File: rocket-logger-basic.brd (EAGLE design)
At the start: 58.5 x 62 mm, 57 parts, among them IC1 CC430F513X, Q2 MOSFET-PCHANNEL, U1 MAX1555, U2 MAX1555, X1 0896BM15A0001, X2 USB-MICROB, X3 SMA-142-0701-801/806

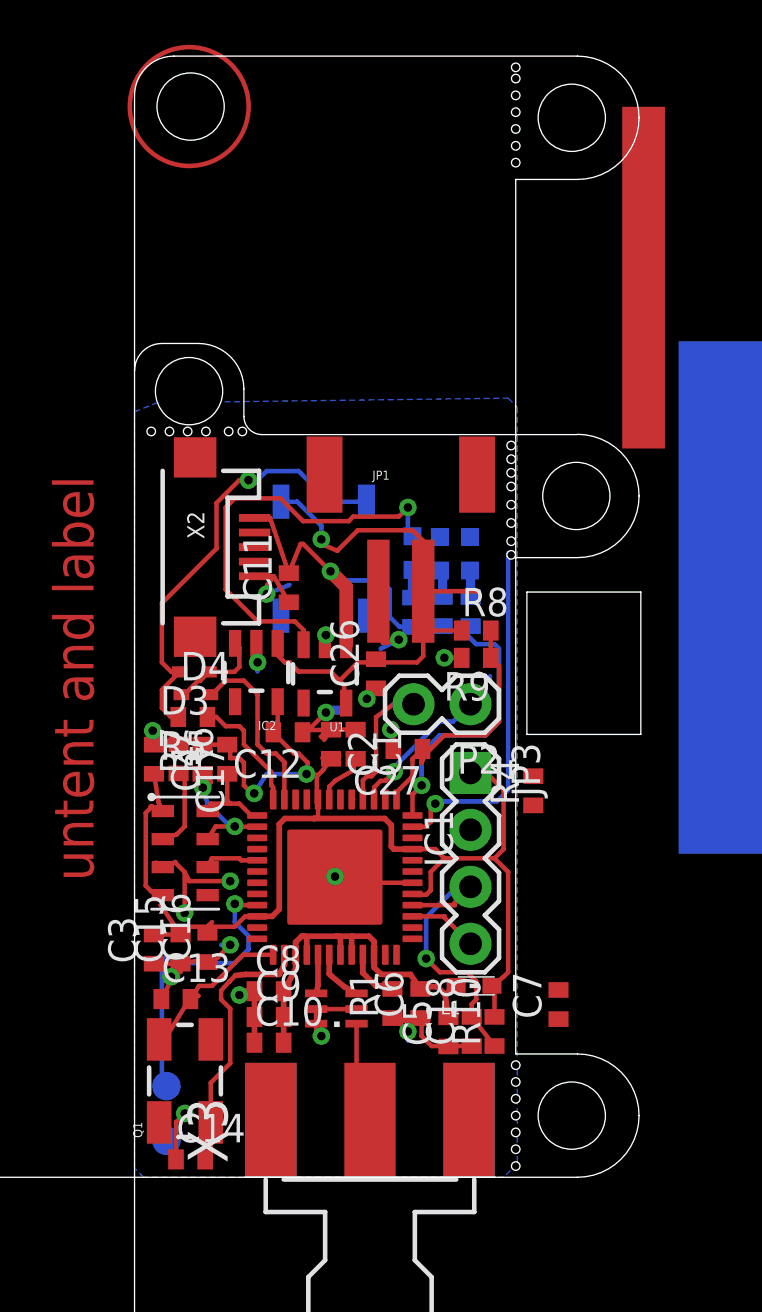
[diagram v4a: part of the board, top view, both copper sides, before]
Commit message: switched to smaller jst connector and done routing
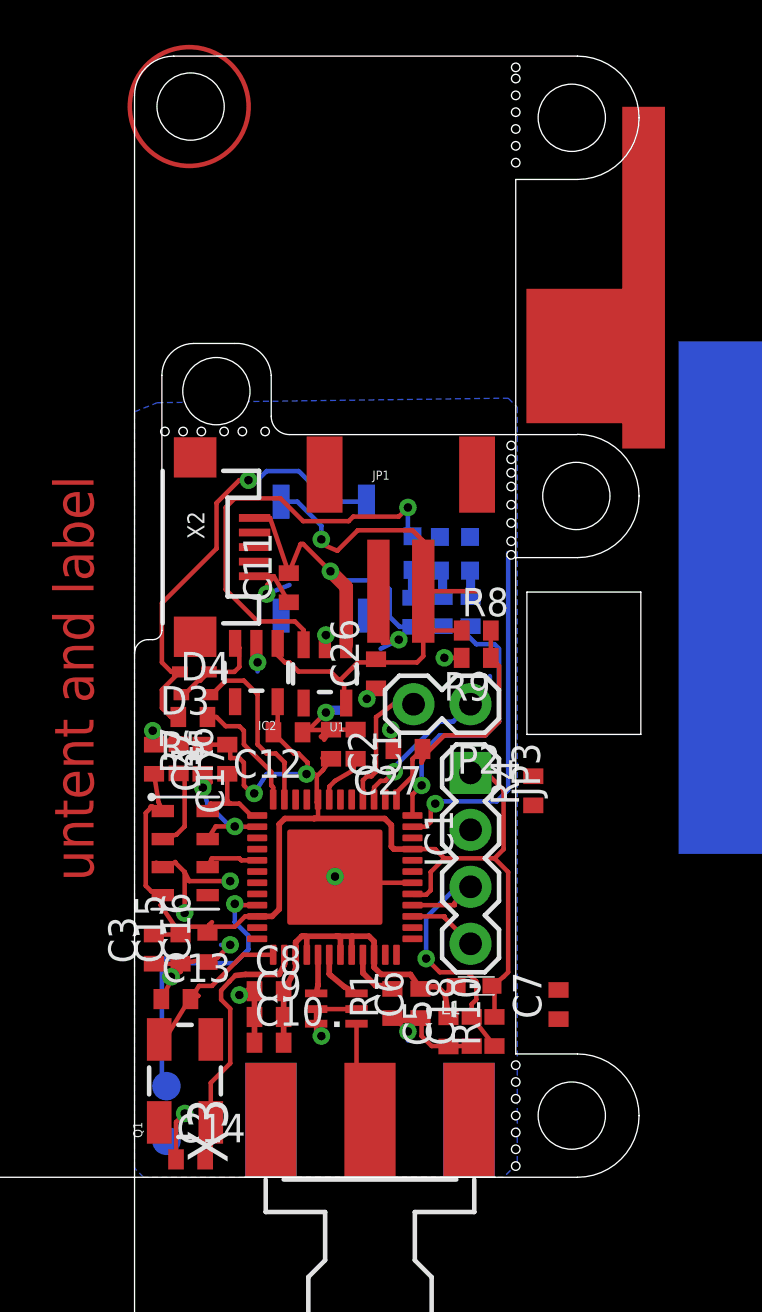
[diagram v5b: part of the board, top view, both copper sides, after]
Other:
- outline, holes or cut-outs redrawn
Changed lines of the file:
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@@
 <text x="10.25" y="37.75" size="1.016" layer="122" ratio="12" rot="MR270">ON</text>
 <text x="8.5" y="37.75" size="1.016" layer="122" ratio="12" rot="MR270">ACT</text>
-<wire x1="0" y1="48.25" x2="0" y2="35.9664" width="0" layer="20"/>
-<wire x1="0" y1="35.9664" x2="0" y2="0" width="0" layer="20"/>
+<wire x1="0" y1="48.25" x2="0" y2="23.368" width="0" layer="20"/>
+<wire x1="0" y1="23.368" x2="0" y2="0" width="0" layer="20"/>
 <wire x1="22.5" y1="2.75" x2="19.75" y2="0" width="0" layer="20" curve="-90"/>
 <wire x1="19.75" y1="5.5" x2="22.5" y2="2.75" width="0" layer="20" curve="-90"/>
@@
 <circle x="2.4384" y="47.752" radius="2.649403125" width="0.2032" layer="1"/>
 <text x="-1.8288" y="13.208" size="1.778" layer="1" rot="R90">untent and label</text>
-<hole x="2.4312" y="35.0588" drill="3"/>
-<wire x1="0" y1="35.9664" x2="1.2192" y2="37.1856" width="0" layer="20" curve="-90"/>
-<wire x1="1.2192" y1="37.1856" x2="2.8448" y2="37.1856" width="0" layer="20"/>
-<wire x1="2.8448" y1="37.1856" x2="4.8768" y2="35.1536" width="0" layer="20" curve="-90"/>
-<wire x1="4.8768" y1="35.1536" x2="4.8768" y2="33.9344" width="0" layer="20"/>
-<wire x1="4.8768" y1="33.9344" x2="5.6896" y2="33.1216" width="0" layer="20" curve="90"/>
-<wire x1="5.6896" y1="33.1216" x2="17.0688" y2="33.1216" width="0" layer="20"/>
+<hole x="3.6504" y="35.0588" drill="3"/>
+<wire x1="2.6416" y1="37.1856" x2="4.4704" y2="37.1856" width="0" layer="20"/>
+<wire x1="4.4704" y1="37.1856" x2="6.096" y2="35.7632" width="0" layer="20" curve="-90"/>
+<wire x1="6.096" y1="35.7632" x2="6.096" y2="33.9344" width="0" layer="20"/>
+<wire x1="6.096" y1="33.9344" x2="6.9088" y2="33.1216" width="0" layer="20" curve="90"/>
+<wire x1="6.9088" y1="33.1216" x2="17.0688" y2="33.1216" width="0" layer="20"/>
+<hole x="5.824" y="33.2612" drill="0.381"/>
 <hole x="4.808" y="33.2612" drill="0.381"/>
-<hole x="4.1984" y="33.2612" drill="0.381"/>
-<hole x="3.1824" y="33.2612" drill="0.381"/>
-<hole x="2.3696" y="33.2612" drill="0.381"/>
-<hole x="1.5568" y="33.2612" drill="0.381"/>
-<hole x="0.744" y="33.2612" drill="0.381"/>
+<hole x="3.9952" y="33.2612" drill="0.381"/>
+<hole x="2.9792" y="33.2612" drill="0.381"/>
+<hole x="2.1664" y="33.2612" drill="0.381"/>
+<hole x="1.3536" y="33.2612" drill="0.381"/>
 <wire x1="19.75" y1="33.1208" x2="17" y2="33.1208" width="0" layer="20"/>
 <wire x1="19.75" y1="33.1344" x2="22.5" y2="30.3844" width="0" layer="20" curve="-90"/>
@@
 <dimension x1="0" y1="0" x2="0" y2="33.1216" x3="-20.7264" y3="16.5608" layer="16"/>
 <dimension x1="0" y1="0" x2="17.0688" y2="0" x3="8.5344" y3="-15.6464" layer="16"/>
+<rectangle x1="17.4752" y1="33.6296" x2="21.9964" y2="39.624" layer="1" rot="R180"/>
+<dimension x1="0" y1="0" x2="0" y2="37.1856" x3="-27.2288" y3="18.5928" layer="16"/>
+<wire x1="1.2192" y1="24.384" x2="0.8128" y2="23.9776" width="0" layer="20" curve="-90"/>
+<wire x1="0.8128" y1="23.9776" x2="0.6096" y2="23.9776" width="0" layer="20"/>
+<wire x1="0.6096" y1="23.9776" x2="0" y2="23.368" width="0" layer="20" curve="90"/>
+<wire x1="1.2192" y1="24.384" x2="1.2192" y2="35.7632" width="0" layer="20"/>
+<wire x1="1.2192" y1="35.7632" x2="2.6416" y2="37.1856" width="0" layer="20" curve="-90"/>
 </plain>
 <attributes>

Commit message: some routing done, changed lipo charger
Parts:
- removed U1: MAX1555, SparkFun:SOT23-5
- added C19: (no value), resistor:C0402
- added R13: (no value), rcl:R0402
- added U$1: JST-ZR-2, Mine:JST-ZR-2
- added U$2: JST-ZR-2SMD, Mine:JST-ZR-2-SMD
- added U3: MCP73831, SparkFun-PowerIC:SOT23-5
- moved JP1 29.6 mm to (34.8, 48.5)
- moved C27 6.10 mm to (15.2, 24.4)
- moved LED1 4.72 mm to (12.0, 24.2), turned to 270 degrees
- moved S2 3.41 mm to (5.53, 29.4), turned to 180 degrees
- moved LED2 2.96 mm to (12.0, 25.4), turned to 270 degrees
- moved C12 2.54 mm to (7.60, 22.3), turned to 90 degrees
- moved R11 2.20 mm to (14.2, 26.4), turned to 180 degrees
- moved C26 1.94 mm to (8.84, 22.3)
- moved LED3 1.48 mm to (12.0, 26.4), turned to 270 degrees
- moved R2 1.36 mm to (14.2, 24.1), turned to 0 degrees
- moved R8 1.22 mm to (15.2, 25.6)
- moved C11 1.12 mm to (7.59, 25.4)
- moved R3 0.46 mm to (14.2, 25.3), turned to 0 degrees
- moved R6 0.41 mm to (4.54, 18.6)
- moved IC2 0.20 mm to (5.43, 22.3)
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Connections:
- new net N$1: R13.1, U3.5
- net +3V3: now also C19.2
- net GND: now also C19.1, R13.2, U$1.2, U$2.2, U3.2; no longer U1.2
- net N$18: now also U3.4; no longer U1.1
- net N$19: now also U3.1; no longer U1.3
- net N$2: now also U$1.1, U$2.1, U3.3; no longer U1.5
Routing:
- net N$19: track 18.9 -> 0.00 mm, vias 1 -> 0
- net GND: track 54.0 -> 60.2 mm, vias 18 -> 16
- net N$24: track 19.9 -> 25.4 mm
- net N$18: track 15.6 -> 19.3 mm
- net +3V3: track 62.3 -> 64.0 mm
- net N$10: track 1.30 -> 0.00 mm
- net N$2: track 26.7 -> 28.0 mm
- net N$15: track 1.24 -> 0.00 mm
- net N$9: track 1.20 -> 0.00 mm
- net N$17: track 15.9 -> 14.7 mm
- net N$1: track 0.00 -> 0.99 mm
- net N$12: track 5.90 -> 5.30 mm
- net N$11: track 6.50 -> 6.97 mm, vias 1 -> 0

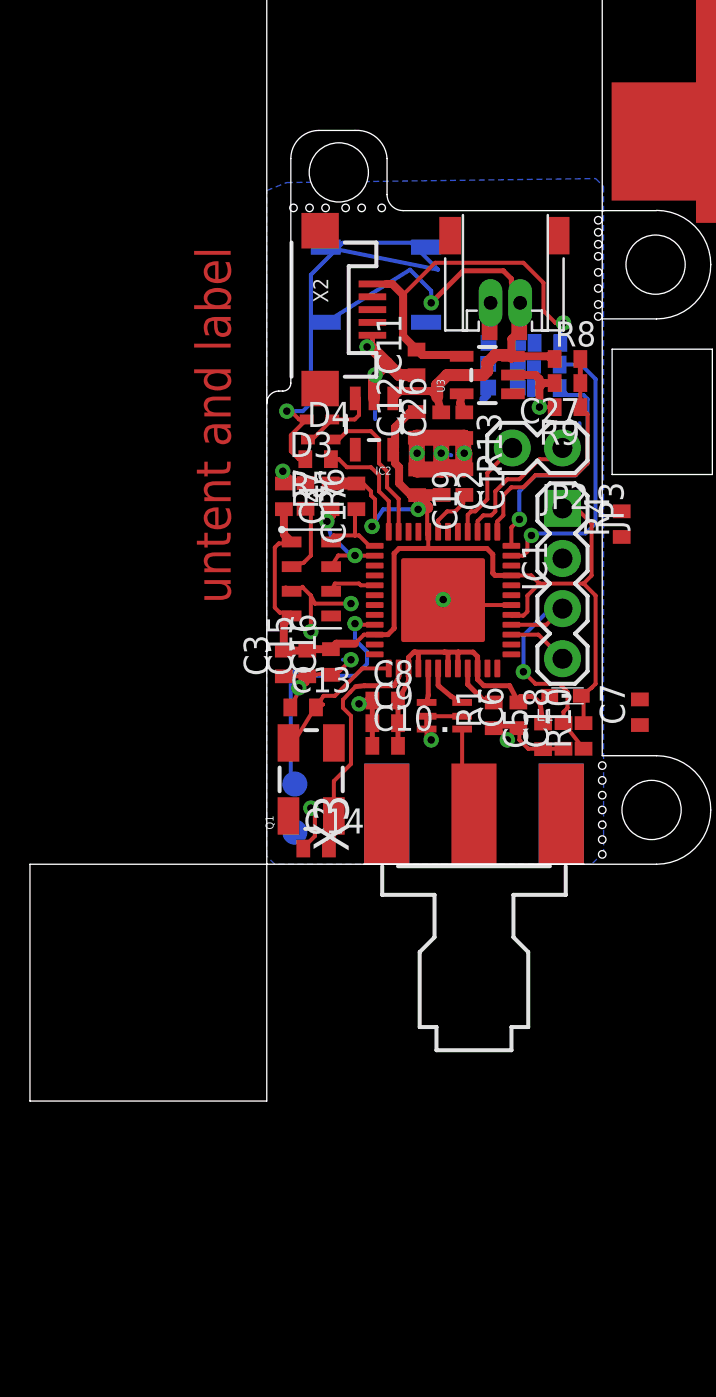
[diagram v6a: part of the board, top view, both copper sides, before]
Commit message: moved leds and done silk layer
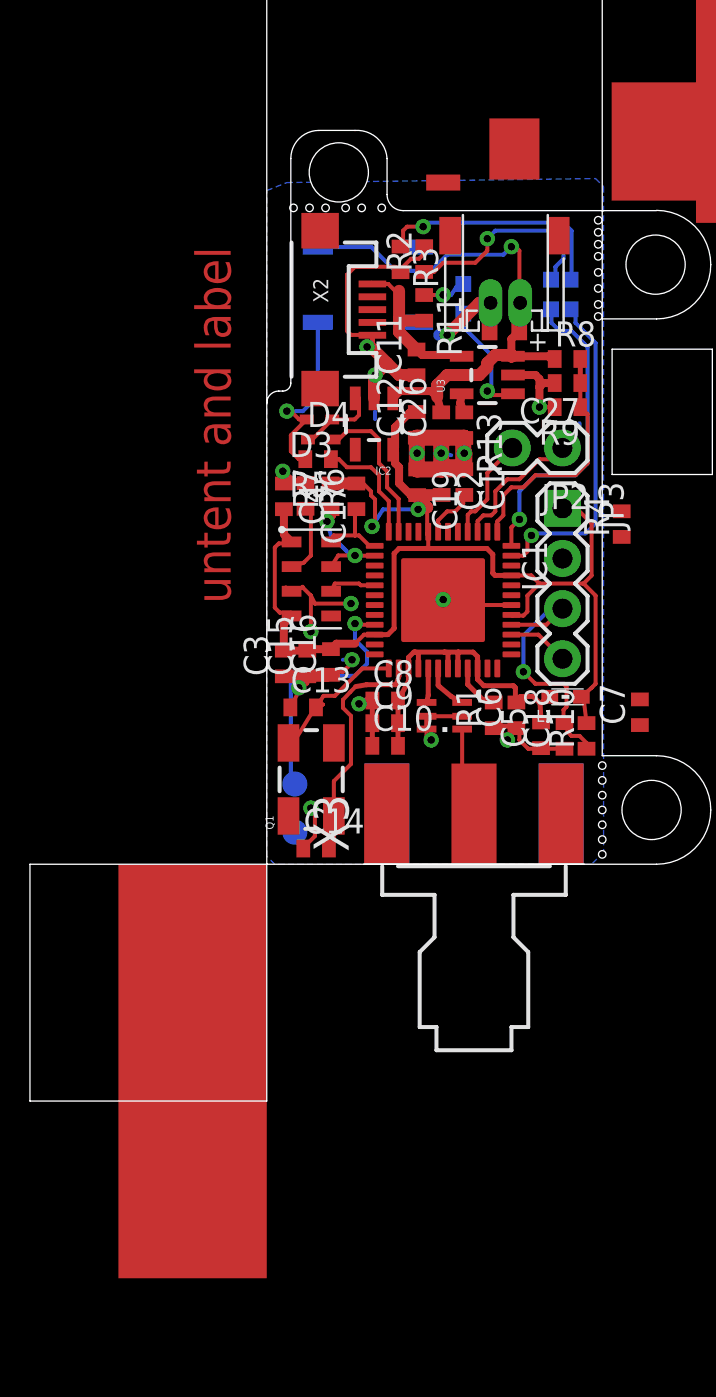
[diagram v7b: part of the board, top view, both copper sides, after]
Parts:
- moved R3 9.13 mm to (6.78, 30.7), flipped to the top, turned to 270 degrees
- moved R2 9.02 mm to (7.97, 30.7), flipped to the top, turned to 90 degrees
- moved R11 6.50 mm to (7.98, 28.2), flipped to the top, turned to 270 degrees
- moved LED1 5.31 mm to (14.4, 28.9), turned to 0 degrees
- moved LED2 4.91 mm to (15.4, 28.9), turned to 0 degrees
- moved LED3 3.02 mm to (9.96, 28.7), turned to 180 degrees
- moved S2 0.41 mm to (5.13, 29.4)
- moved R10 0.15 mm to (16.2, 6.50)
- moved C5 0.11 mm to (13.9, 6.53)
- moved C6 0.10 mm to (12.6, 7.55)
- moved C18 0.05 mm to (15.1, 6.50)
- moved L1 0.05 mm to (15.2, 8.48)
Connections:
- removed net N$17: IC1.47, R3.1
- new net N$28: IC1.47, LED2.A
- net GND: now also R2.2, R3.2; no longer LED1.C, LED2.C
- net N$10: now also LED2.C, R3.1; no longer LED2.A, R3.2
- net N$16: now also LED1.A; no longer R2.1
- net N$2: now also S2.3; no longer S2.1
- net N$24: now also S2.1; no longer S2.3
- net N$9: now also LED1.C, R2.1; no longer LED1.A, R2.2
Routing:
- net N$28: track 0.00 -> 16.7 mm, vias 0 -> 1
- net N$24: track 25.4 -> 9.65 mm
- net N$17: track 14.7 -> 0.00 mm, vias 1 -> 0
- net GND: track 60.2 -> 72.8 mm, vias 16 -> 17
- net N$10: track 0.00 -> 12.4 mm, vias 0 -> 1
- net N$9: track 0.00 -> 11.1 mm, vias 0 -> 1
- net N$18: track 19.3 -> 8.66 mm, vias 1 -> 0
- net N$19: track 0.00 -> 6.01 mm, vias 0 -> 1
- net N$16: track 12.3 -> 15.9 mm
- net N$15: track 0.00 -> 2.48 mm, vias 0 -> 1
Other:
- board text added: "+"
- board text added: "CHG"
- board text added: "ON/OFF"
- board text added: "PWR"
